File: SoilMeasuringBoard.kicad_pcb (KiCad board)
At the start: 2 copper layers, 22.5 x 100 mm, 35 parts, among them J1 USB_B_Micro, J2 BATT_CONN, J3 Conn_01x07, Q1 Q_NMOS_GSD, Q2 DMP3099L-13, Q3 DMP3099L-13, U1 RFD77101, U2 MCP73811T-420I-OT, U3 TLV74130, U4 DS18B20U

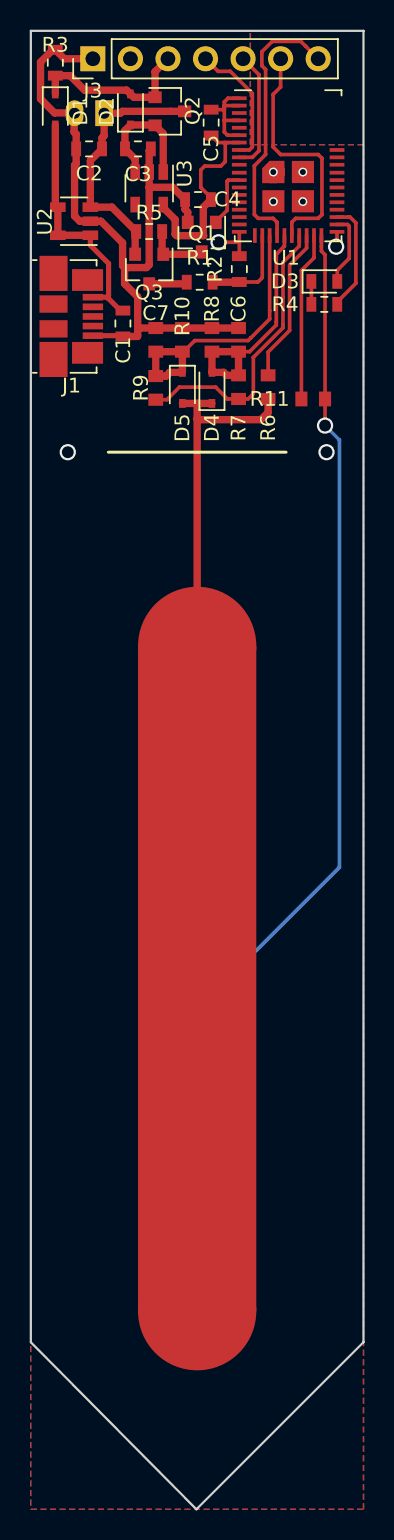
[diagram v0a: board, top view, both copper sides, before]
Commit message: add flash memory
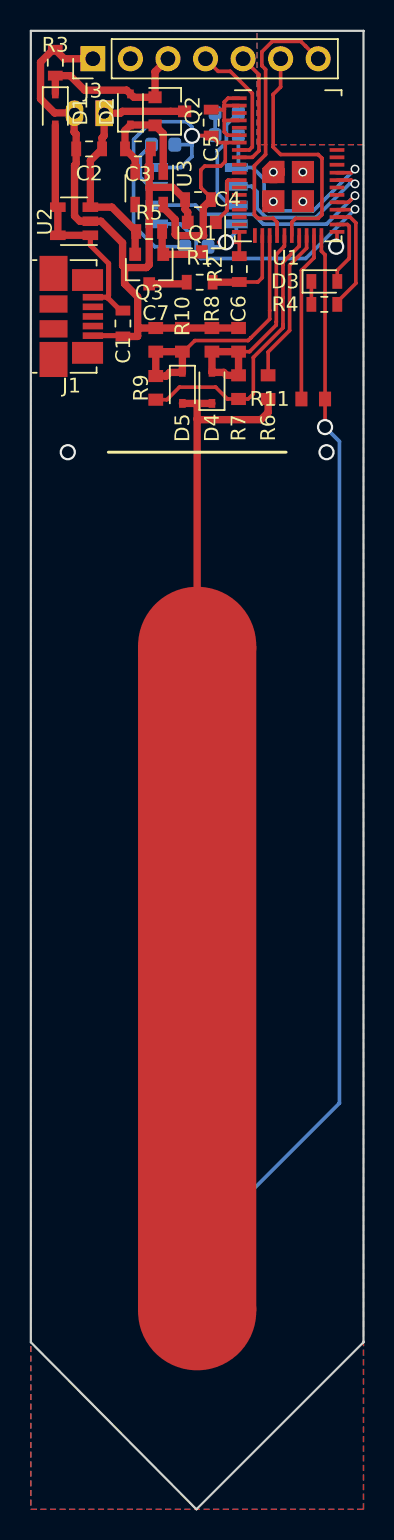
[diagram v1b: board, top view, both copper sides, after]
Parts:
- added C8: 0.1u, Capacitor_SMD:C_0603_1608Metric, B.Cu at (148.8, 52.8)
- added R12: 100k, Resistor_SMD:R_0603_1608Metric, B.Cu at (146.6, 45.9)
- added R13: 100k, Resistor_SMD:R_0603_1608Metric, B.Cu at (150.9, 43.8)
- added R14: 100k, Resistor_SMD:R_0603_1608Metric, B.Cu at (150.9, 45.3)
- added U5: SST26VF016B, Package_SO:SOIC-8_3.9x4.9mm_P1.27mm, B.Cu at (148.8, 49.4)
- R11: value R -> 4.7k
- R4: value R -> 47
- moved G*** 29.6 mm to (148.9, 78.5)
- moved U4 15.9 mm to (149.0, 118.0)
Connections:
- U1 pad 33: (no net) -> /SPI_MOSI
- U1 pad 34: (no net) -> /SPI_SCK
- U1 pad 37: (no net) -> /SPI_MISO
- U1 pad 38: (no net) -> /SPI_SS
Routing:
- net VDD: track 14.9 -> 39.6 mm, vias 0 -> 1
- net /SPI_MOSI: track 0.00 -> 17.6 mm, vias 0 -> 1
- net /SPI_SCK: track 0.00 -> 16.2 mm, vias 0 -> 1
- net /TEMP_DATA: track 56.4 -> 72.2 mm
- net /SPI_SS: track 0.00 -> 15.5 mm, vias 0 -> 1
- net /SPI_MISO: track 0.00 -> 11.8 mm, vias 0 -> 1
- net Net-(R13-Pad2): track 0.00 -> 7.64 mm
- net Net-(R12-Pad2): track 0.00 -> 3.86 mm
- net GND: track 62.6 -> 65.5 mm
